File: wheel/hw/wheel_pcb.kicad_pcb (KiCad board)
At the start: 2 copper layers, 36 x 67 mm, 65 parts, among them J2 DEBUG, J3 IO_C, J4 CAR, J5 IO_B, J6 IO_A, SW1 TERM, U1 LPC11C24FBD48, U2 TPS62175, U3 TLV70233_SOT23-5, U4 SP4065-08ATG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

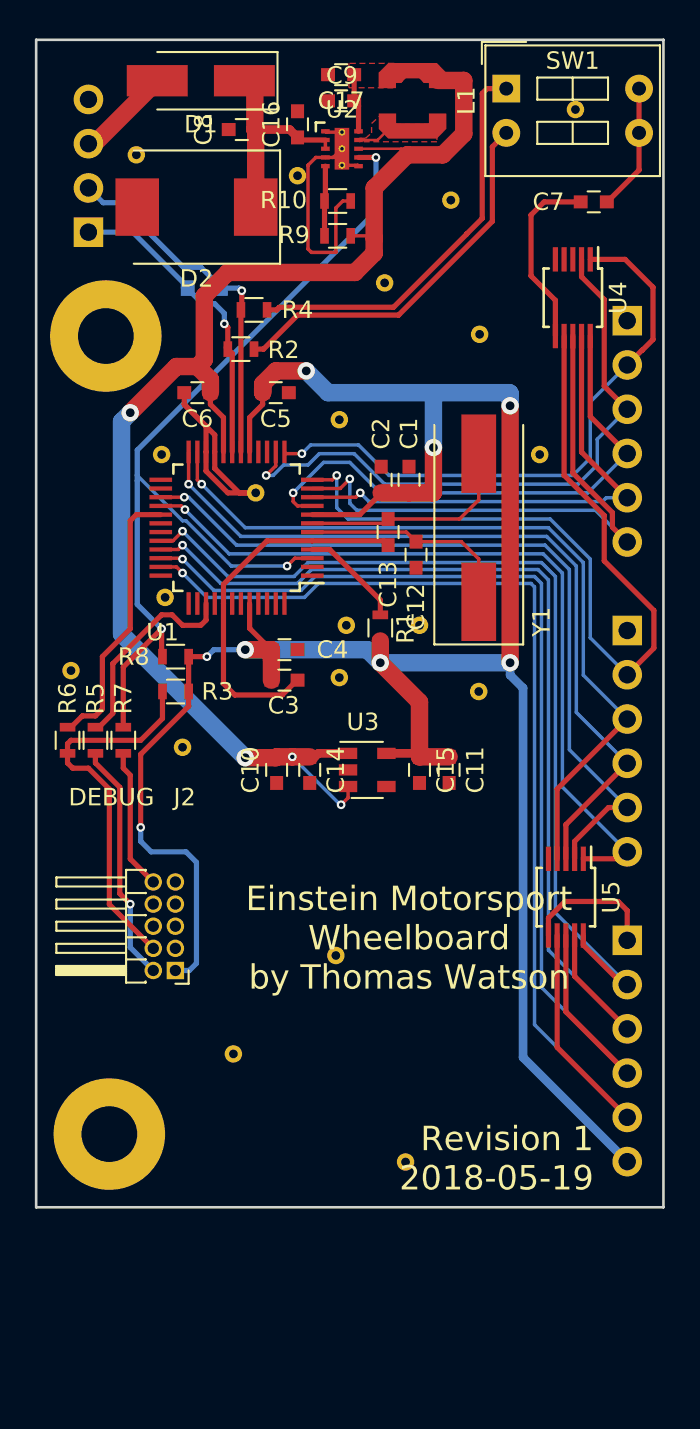
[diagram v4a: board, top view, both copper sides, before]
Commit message: fix various silkscreen related transgressions
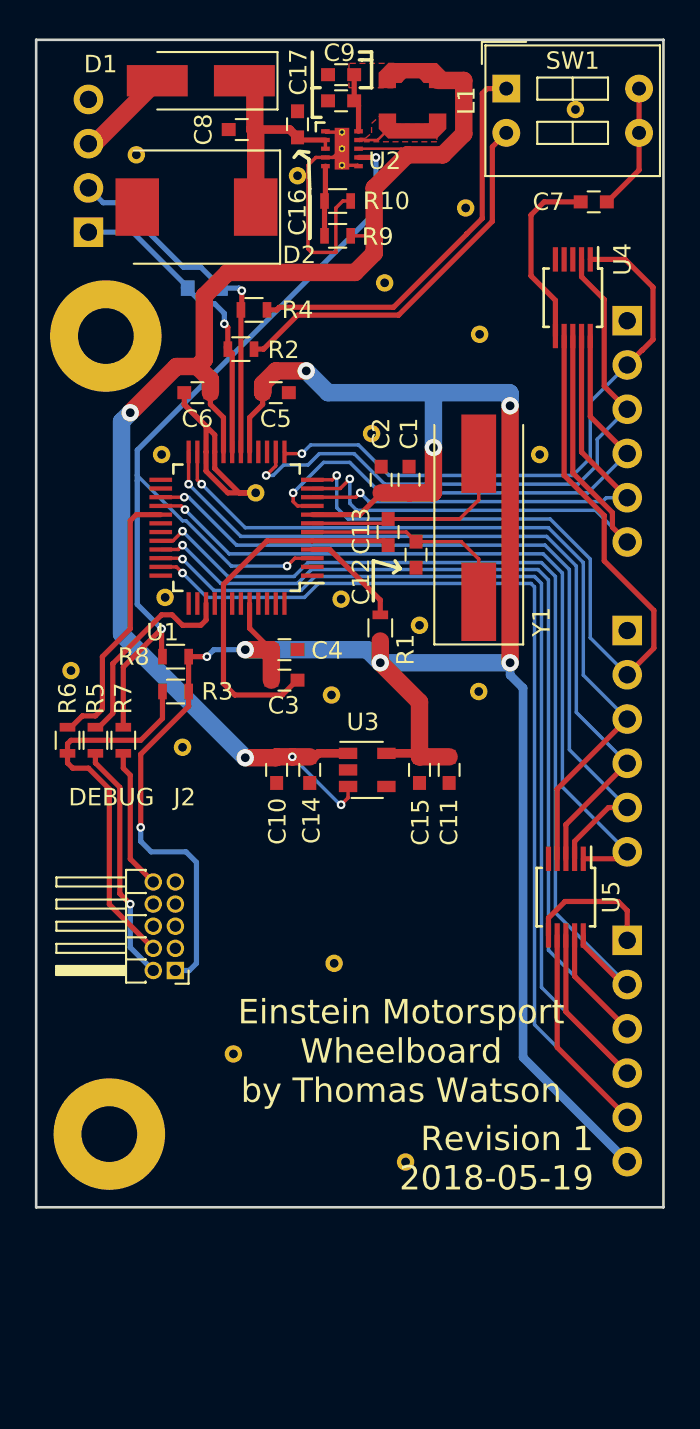
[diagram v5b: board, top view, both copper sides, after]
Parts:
- moved REF** 2.02 mm to (242.2, 77.6)
- moved REF** 1.53 mm to (240.5, 87.1)
- moved REF** 1.10 mm to (239.9, 92.6)
- moved REF** 0.96 mm to (247.7, 64.7)
- moved REF** 0.46 mm to (240.1, 108.0)
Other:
- board text added: "3.3V:6 A4:5 A3:4 A2:3 A1:2 GND:1"
- board text added: "B5:6 B4:5 B3:4 B2:3 B1:2 GND:1"
- board text added: "C5:6 C4:5 C3:4 C2:3 C1:2 GND:1"
- board text added: "DIP Switch 1: TERMINATE CANL 2: TERMINATE CANH"
- board text removed: "1:GND 2:A1 3:A2 4:A3 5:A4 6:3.3V"
- board text removed: "1:GND 2:B1 3:B2 4:B3 5:B4 6:B5"
- board text removed: "1:GND 2:C1 3:C2 4:C3 5:C4 6:C5"
- board text removed: "DIP Switch 1: TERMINATE CANL 2: TERMINATE CANH 3: NOT USED 4: NOT USED"
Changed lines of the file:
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@@
     (area 222.924999 54.924999 259.075001 122.075001)
     (thickness 1.6)
-    (drawings 11)
+    (drawings 32)
     (tracks 475)
     (zones 0)
@@
     (34 B.Paste user)
     (35 F.Paste user)
-    (36 B.SilkS user hide)
-    (37 F.SilkS user hide)
+    (36 B.SilkS user)
+    (37 F.SilkS user)
     (38 B.Mask user)
     (39 F.Mask user)
@@
   )
   (setup
-    (last_trace_width 0.5)
+    (last_trace_width 0.15)
     (user_trace_width 0.2)
     (user_trace_width 0.3)
@@
   )
   (module custom_footprints:a_via locked (layer B.Cu)
-    (at 240.2 107.55)
+    (at 240.1 108)
     (fp_text reference REF** (at 0 -0.5) (layer B.SilkS) hide
       (effects (font (size 1 1) (thickness 0.15)) (justify mirror))
@@
   )
   (module custom_footprints:a_via locked (layer B.Cu)
-    (at 240.4 91.6)
+    (at 239.95 92.6)
     (fp_text reference REF** (at 0 -0.5) (layer B.SilkS) hide
       (effects (font (size 1 1) (thickness 0.15)) (justify mirror))
@@
   )
   (module custom_footprints:a_via locked (layer B.Cu)
-    (at 240.8 88.6)
+    (at 240.5 87.1)
     (fp_text reference REF** (at 0 -0.5) (layer B.SilkS) hide
       (effects (font (size 1 1) (thickness 0.15)) (justify mirror))
@@
   )
   (module custom_footprints:a_via locked (layer B.Cu)
-    (at 240.4 76.8)
+    (at 242.25 77.6)
     (fp_text reference REF** (at 0 -0.5) (layer B.SilkS) hide
       (effects (font (size 1 1) (thickness 0.15)) (justify mirror))
@@
   )
   (module custom_footprints:a_via locked (layer F.Cu)
-    (at 246.8 64.2)
+    (at 247.65 64.65)
     (fp_text reference REF** (at 0 0.5) (layer F.SilkS) hide
       (effects (font (size 1 1) (thickness 0.15)))
@@
     (tags "capacitor 0603")
     (attr smd)
-    (fp_text reference C4 (at 2.75 0) (layer F.SilkS)
+    (fp_text reference C4 (at 2.45 0.05) (layer F.SilkS)
       (effects (font (size 1 1) (thickness 0.15)))
     )
@@
     (tags "capacitor 0603")
     (attr smd)
-    (fp_text reference C9 (at -0.05 1.45 180) (layer F.SilkS)
+    (fp_text reference C9 (at 0.1 2.75 180) (layer F.SilkS)
       (effects (font (size 1 1) (thickness 0.15)))
     )
@@
     (tags "capacitor 0603")
     (attr smd)
-    (fp_text reference C10 (at 0 1.5 270) (layer F.SilkS)
+    (fp_text reference C10 (at 2.95 -0.05 270) (layer F.SilkS)
       (effects (font (size 1 1) (thickness 0.15)))
     )
@@
     (tags "capacitor 0603")
     (attr smd)
-    (fp_text reference C11 (at 0 -1.5 270) (layer F.SilkS)
+    (fp_text reference C11 (at 3 0 270) (layer F.SilkS)
       (effects (font (size 1 1) (thickness 0.15)))
     )
@@
     (tags "capacitor 0603")
     (attr smd)
-    (fp_text reference C12 (at -3 0 90) (layer F.SilkS)
+    (fp_text reference C12 (at -1.55 -3.15 90) (layer F.SilkS)
       (effects (font (size 1 1) (thickness 0.15)))
     )
@@
     (tags "capacitor 0603")
     (attr smd)
-    (fp_text reference C13 (at -3 0 90) (layer F.SilkS)
+    (fp_text reference C13 (at 0.05 -1.55 90) (layer F.SilkS)
       (effects (font (size 1 1) (thickness 0.15)))
     )
@@
     (tags "resistor 0603")
     (attr smd)
-    (fp_text reference R1 (at 0 -1.45 270) (layer F.SilkS)
+    (fp_text reference R1 (at 1.25 -1.45 270) (layer F.SilkS)
       (effects (font (size 1 1) (thickness 0.15)))
     )
@@
     (tags "resistor 0603")
     (attr smd)
-    (fp_text reference R9 (at 2.5 0.05 360) (layer F.SilkS)
+    (fp_text reference R9 (at -2.3 -0.05 360) (layer F.SilkS)
       (effects (font (size 1 1) (thickness 0.15)))
     )
@@
     (tags "resistor 0603")
     (attr smd)
-    (fp_text reference R10 (at -3.1 -0.05 180) (layer F.SilkS)
+    (fp_text reference R10 (at 2.8 0 180) (layer F.SilkS)
       (effects (font (size 1 1) (thickness 0.15)))
     )
@@
     (solder_mask_margin 0.07)
     (solder_paste_ratio -0.17)
-    (fp_text reference U2 (at 0 -2.25) (layer F.SilkS)
+    (fp_text reference U2 (at 2.45 0.7) (layer F.SilkS)
       (effects (font (size 1 1) (thickness 0.15)))
     )
@@
     (tags "capacitor 0603")
     (attr smd)
-    (fp_text reference C14 (at 0 -1.5 270) (layer F.SilkS)
+    (fp_text reference C14 (at 2.9 -0.1 270) (layer F.SilkS)
       (effects (font (size 1 1) (thickness 0.15)))
     )
@@
     (tags "capacitor 0603")
     (attr smd)
-    (fp_text reference C15 (at 0 -1.5 270) (layer F.SilkS)
+    (fp_text reference C15 (at 3 -0.05 270) (layer F.SilkS)
       (effects (font (size 1 1) (thickness 0.15)))
     )
@@
     (tags "capacitor 0603")
     (attr smd)
-    (fp_text reference C16 (at 0 -1.5 90) (layer F.SilkS)
+    (fp_text reference C16 (at -5.05 0 90) (layer F.SilkS)
       (effects (font (size 1 1) (thickness 0.15)))
     )
@@
     (tags "capacitor 0603")
     (attr smd)
-    (fp_text reference C17 (at 0 -1.5 180) (layer F.SilkS)
+    (fp_text reference C17 (at 2.45 0.15 450) (layer F.SilkS)
       (effects (font (size 1 1) (thickness 0.15)))
     )
@@
     (tags "Diode SMA (DO-214AC) Handsoldering")
     (attr smd)
-    (fp_text reference D1 (at 0 -2.5 180) (layer F.SilkS)
+    (fp_text reference D1 (at 5.75 0.95 180) (layer F.SilkS)
       (effects (font (size 1 1) (thickness 0.15)))
     )
@@
     (tags "Diode SMC (DO-214AB)")
     (attr smd)
-    (fp_text reference D2 (at 0 -4.1 180) (layer F.SilkS)
+    (fp_text reference D2 (at -5.9 -2.75 180) (layer F.SilkS)
       (effects (font (size 1 1) (thickness 0.15)))
     )
@@
     (tags SOT-23)
     (attr smd)
-    (fp_text reference D3 (at 0 2.5 270) (layer B.SilkS)
+    (fp_text reference D3 (at 2.55 0.4 360) (layer B.SilkS)
       (effects (font (size 1 1) (thickness 0.15)) (justify mirror))
     )
@@
     (tags "SSOP 0.5")
     (attr smd)
-    (fp_text reference U4 (at 0 -2.6 270) (layer F.SilkS)
+    (fp_text reference U4 (at -2.2 -2.85 270) (layer F.SilkS)
       (effects (font (size 1 1) (thickness 0.15)))
     )
@@
     )
   )
-  (gr_text "1:GND\n2:C1\n3:C2\n4:C3\n5:C4\n6:C5" (at 245.2 77.6) (layer B.SilkS)
+  (gr_line (start 243.85 85.35) (end 243.5 85.6) (layer F.SilkS) (width 0.2))
+  (gr_line (start 243.9 85.35) (end 243.6 84.9) (layer F.SilkS) (width 0.2))
+  (gr_line (start 242.35 84.9) (end 243.9 85.35) (layer F.SilkS) (width 0.2))
+  (gr_line (start 242.35 87.2) (end 242.35 84.9) (layer F.SilkS) (width 0.2))
+  (gr_line (start 241.7 56.15) (end 241.55 56.15) (layer F.SilkS) (width 0.2))
+  (gr_line (start 242.25 57.75) (end 241.6 57.75) (layer F.SilkS) (width 0.2))
+  (gr_line (start 242.25 56.15) (end 242.25 57.75) (layer F.SilkS) (width 0.2))
+  (gr_line (start 242.25 56.15) (end 241.7 56.15) (layer F.SilkS) (width 0.2))
+  (gr_line (start 242.25 55.7) (end 242.25 56.15) (layer F.SilkS) (width 0.2))
+  (gr_line (start 241.55 55.7) (end 242.25 55.7) (layer F.SilkS) (width 0.2))
+  (gr_line (start 238.85 59.45) (end 239.35 59.45) (layer F.SilkS) (width 0.2))
+  (gr_line (start 238.85 57.75) (end 238.85 59.45) (layer F.SilkS) (width 0.2))
+  (gr_line (start 238.9 57.75) (end 238.85 57.75) (layer F.SilkS) (width 0.2))
+  (gr_line (start 239.3 57.75) (end 238.9 57.75) (layer F.SilkS) (width 0.2))
+  (gr_line (start 238.85 55.7) (end 238.85 57.85) (layer F.SilkS) (width 0.2))
+  (gr_line (start 238.1 61.4) (end 238.65 61.45) (layer F.SilkS) (width 0.2))
+  (gr_line (start 238.05 61.45) (end 237.8 61.75) (layer F.SilkS) (width 0.2))
+  (gr_line (start 238.65 61.85) (end 238.05 61.45) (layer F.SilkS) (width 0.2))
+  (gr_line (start 238.7 63.55) (end 238.65 61.85) (layer F.SilkS) (width 0.2))
+  (gr_line (start 238.7 66.4) (end 238.7 63.95) (layer F.SilkS) (width 0.2))
+  (gr_line (start 238.7 63.55) (end 238.7 66.4) (layer F.SilkS) (width 0.2))
+  (gr_text "C5:6\nC4:5\nC3:4\nC2:3\nC1:2\nGND:1" (at 243.5 77.6 180) (layer B.SilkS)
+    (effects (font (size 1.5 1.5) (thickness 0.3)) (justify right mirror))
+  )
+  (gr_text "1:CANH\n2:CANL\n3:+12V\n4:GND" (at 240.1 62.4 180) (layer B.SilkS)
     (effects (font (size 1.5 1.5) (thickness 0.3)) (justify left mirror))
   )
-  (gr_text "1:CANH\n2:CANL\n3:+12V\n4:GND" (at 238.8 62.4 180) (layer B.SilkS)
-    (effects (font (size 1.5 1.5) (thickness 0.3)) (justify left mirror))
-  )
-  (gr_text "1:GND\n2:A1\n3:A2\n4:A3\n5:A4\n6:3.3V" (at 245.2 113) (layer B.SilkS)
-    (effects (font (size 1.5 1.5) (thickness 0.3)) (justify left mirror))
-  )
-  (gr_text "1:GND\n2:B1\n3:B2\n4:B3\n5:B4\n6:B5" (at 245.2 95.2) (layer B.SilkS)
-    (effects (font (size 1.5 1.5) (thickness 0.3)) (justify left mirror))
+  (gr_text "3.3V:6\nA4:5\nA3:4\nA2:3\nA1:2\nGND:1" (at 243.5 113 180) (layer B.SilkS)
+    (effects (font (size 1.5 1.5) (thickness 0.3)) (justify right mirror))
+  )
+  (gr_text "B5:6\nB4:5\nB3:4\nB2:3\nB1:2\nGND:1" (at 243.5 95.2 180) (layer B.SilkS)
+    (effects (font (size 1.5 1.5) (thickness 0.3)) (justify right mirror))
   )
   (gr_text "Revision 1\n2018-05-19" (at 255 119.2) (layer F.SilkS)
     (effects (font (size 1.4 1.4) (thickness 0.28)) (justify right))
   )
-  (gr_text "Einstein Motorsport\nWheelboard\nby Thomas Watson" (at 244.4 106.55) (layer F.SilkS)
+  (gr_text "Einstein Motorsport\nWheelboard\nby Thomas Watson" (at 243.95 113.05) (layer F.SilkS)
     (effects (font (size 1.4 1.4) (thickness 0.28)))
   )
-  (gr_text "DIP Switch\n1: TERMINATE CANL\n2: TERMINATE CANH\n3: NOT USED\n4: NOT USED" (at 230.35 78.05 90) (layer B.SilkS)
+  (gr_text "DIP Switch\n1: TERMINATE CANL\n2: TERMINATE CANH" (at 226.95 78.05 90) (layer B.SilkS)
     (effects (font (size 1.4 1.4) (thickness 0.28)) (justify left mirror))
   )

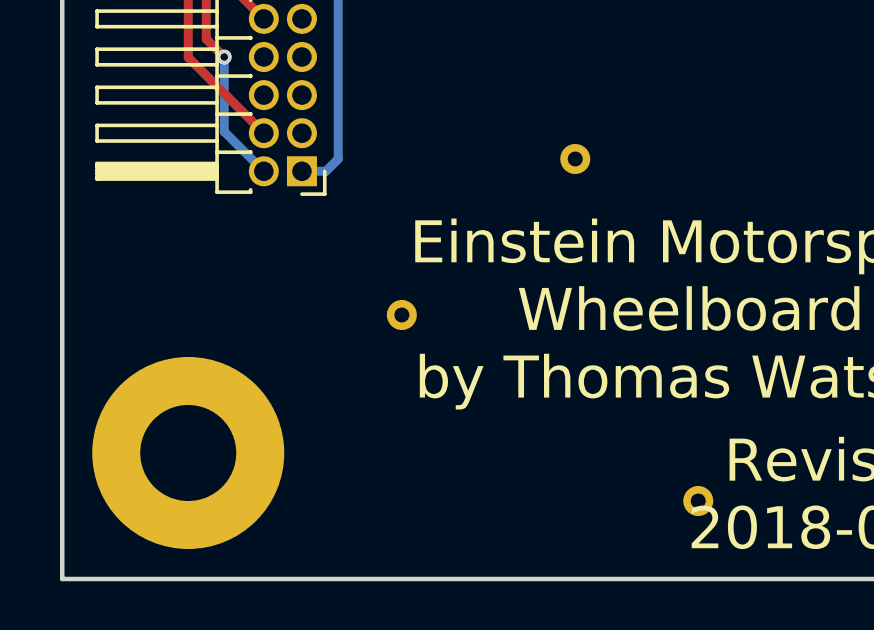
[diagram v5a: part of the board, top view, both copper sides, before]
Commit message: add github link to boards
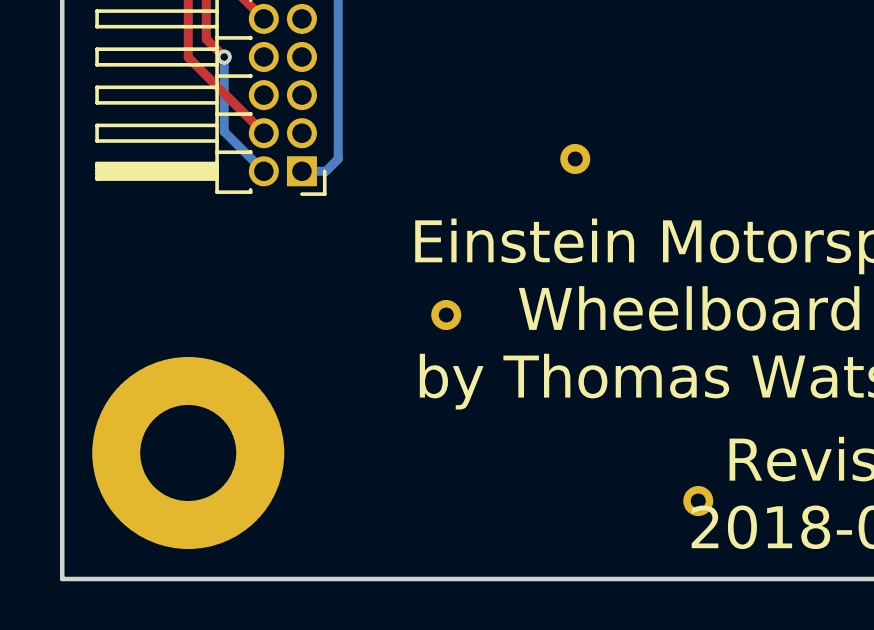
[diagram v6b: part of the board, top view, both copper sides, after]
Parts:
- moved REF** 1.48 mm to (235.8, 113.2)
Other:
- board text added: "https://github.com/tpwrules/emdash"
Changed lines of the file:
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@@
     (area 222.924999 54.924999 259.075001 122.075001)
     (thickness 1.6)
-    (drawings 32)
+    (drawings 33)
     (tracks 475)
     (zones 0)
@@
   )
   (module custom_footprints:a_via locked (layer B.Cu)
-    (at 234.32 113.2 180)
+    (at 235.8 113.2 180)
     (fp_text reference REF** (at 0 -0.5 180) (layer B.SilkS) hide
       (effects (font (size 1 1) (thickness 0.15)) (justify mirror))
@@
     )
   )
+  (gr_text https://github.com/tpwrules/emdash (at 233.6 94.6 90) (layer B.SilkS)
+    (effects (font (size 1.5 1.5) (thickness 0.3)) (justify mirror))
+  )
   (gr_line (start 243.85 85.35) (end 243.5 85.6) (layer F.SilkS) (width 0.2))

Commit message: misc preparations incl better silkscreen and grounding
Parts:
- added REF**: a_via, custom_footprints:a_via, B.Cu at (226.2, 76.0)
- added REF**: a_via, custom_footprints:a_via, B.Cu at (224.2, 69.0)
- added REF**: a_via, custom_footprints:a_via, B.Cu at (231.0, 71.0)
- added REF**: a_via, custom_footprints:a_via, B.Cu at (231.6, 120.8)
- added REF**: a_via, custom_footprints:a_via, B.Cu at (231.6, 113.6)
- added REF**: a_via, custom_footprints:a_via, B.Cu at (224.2, 113.6)
- moved REF** 3.04 mm to (248.4, 67.6)
- moved REF** 0.82 mm to (244.8, 89.4)

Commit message: bump revision to 2 and plot it
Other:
- board text added: "Revision 2 2018-06-23"
- board text removed: "Revision 1 2018-05-19"
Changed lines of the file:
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@@
     (links 162)
     (no_connects 0)
-    (area 222.924999 54.924999 259.075001 122.075001)
+    (area 217.492857 53.825 259.155001 123.025)
     (thickness 1.6)
     (drawings 26)
@@
       (drillshape 0)
       (scaleselection 1)
-      (outputdirectory r1/))
+      (outputdirectory r2/))
   )
   (net 0 "")
@@
     (effects (font (size 1.5 1.5) (thickness 0.3)) (justify right mirror))
   )
-  (gr_text "Revision 1\n2018-05-19" (at 254.4 119.2) (layer F.SilkS)
+  (gr_text "Revision 2\n2018-06-23" (at 254.4 119.2) (layer F.SilkS)
     (effects (font (size 1.4 1.4) (thickness 0.28)) (justify right))
   )
